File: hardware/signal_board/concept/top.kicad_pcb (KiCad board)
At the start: 2 copper layers, 85 x 115 mm, 288 parts, among them J1 Conn_01x04, J2 USB_OTG, J3 Conn_01x02, J4 Barrel_Jack_Switch, Q1 Q_NMOS_GDS, Q10 Q_NMOS_GDS, Q11 Q_NMOS_GDS, Q12 Q_NMOS_GDS, Q13 Q_NMOS_GDS, Q14 Q_PMOS_GDS, Q15 Q_NMOS_GDS, Q16 Q_PMOS_GDS, Q17 Q_NMOS_GDS, Q18 Q_NMOS_GDS, Q19 Q_NMOS_GDS, Q2 Q_NMOS_GDS, Q20 Q_NMOS_GDS, Q21 Q_NMOS_GDS, Q22 Q_NMOS_GDS, Q3 Q_PMOS_GDS, Q4 Q_NMOS_GDS, Q5 Q_PMOS_GDS, Q6 Q_NMOS_GDS, Q7 Q_NMOS_GDS, Q8 Q_NMOS_GDS, Q9 Q_NMOS_GDS, SW1 SW_Push, SW2 SW_Push, SW3 SW_Push, SW4 SW_Push, U1 STM32F103R(F-G)Tx_u, U10 L5973D, U11 LM3488MM, U12 AMS1117-3.3, U13 AMS1117, U14 LM324, U15 LM324, U16 MCP6001-OT, U17 MCP6001-OT, U18 ADS1118IDGS, U19 LM358, U2 XC6SLX9-TQG144, U20 IR1155S, U21 IR1155S, U22 IR1155S, U23 IR1155S, U3 W25Q32JVSS, U4 MCP6002-xMS, U5 LM324, U6 LM324, U7 MCP6001-OT, U8 MCP6001-OT, U9 ADS1118IDGS, Y1 8MHz

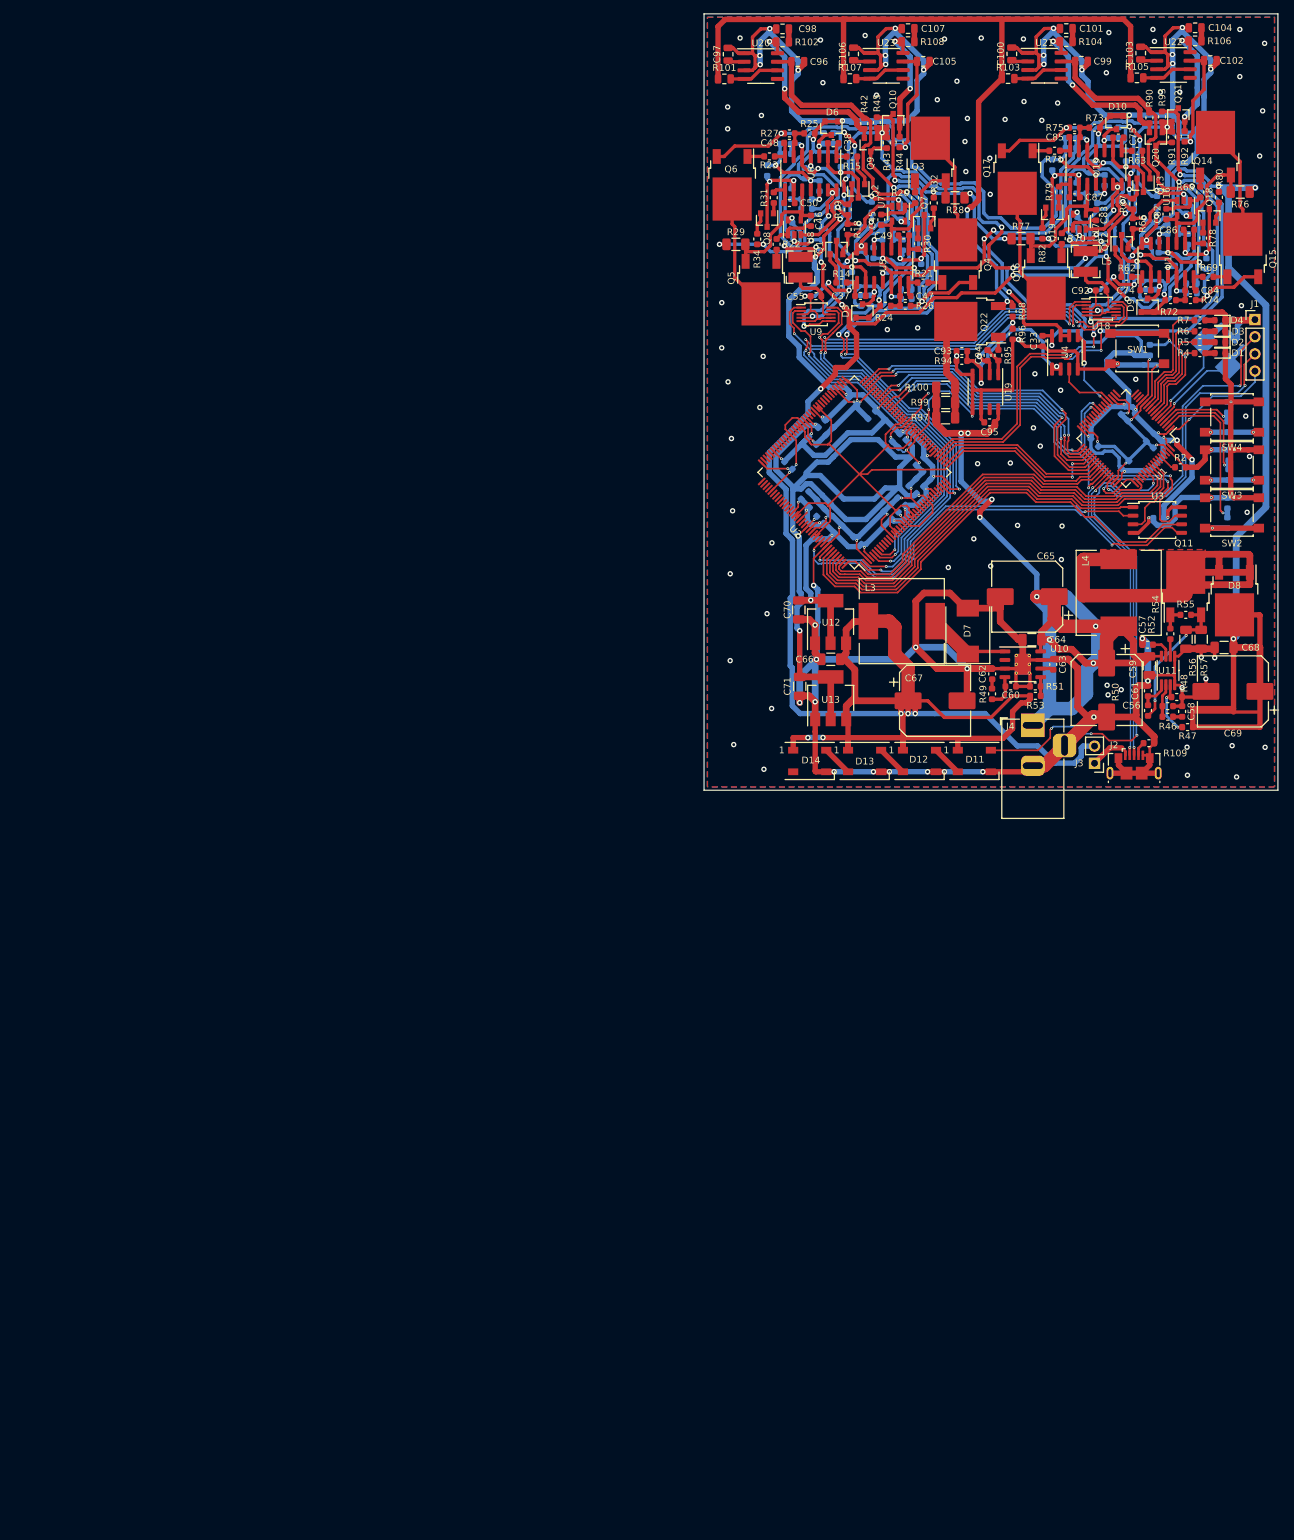
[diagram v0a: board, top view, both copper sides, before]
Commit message: Add priduction board
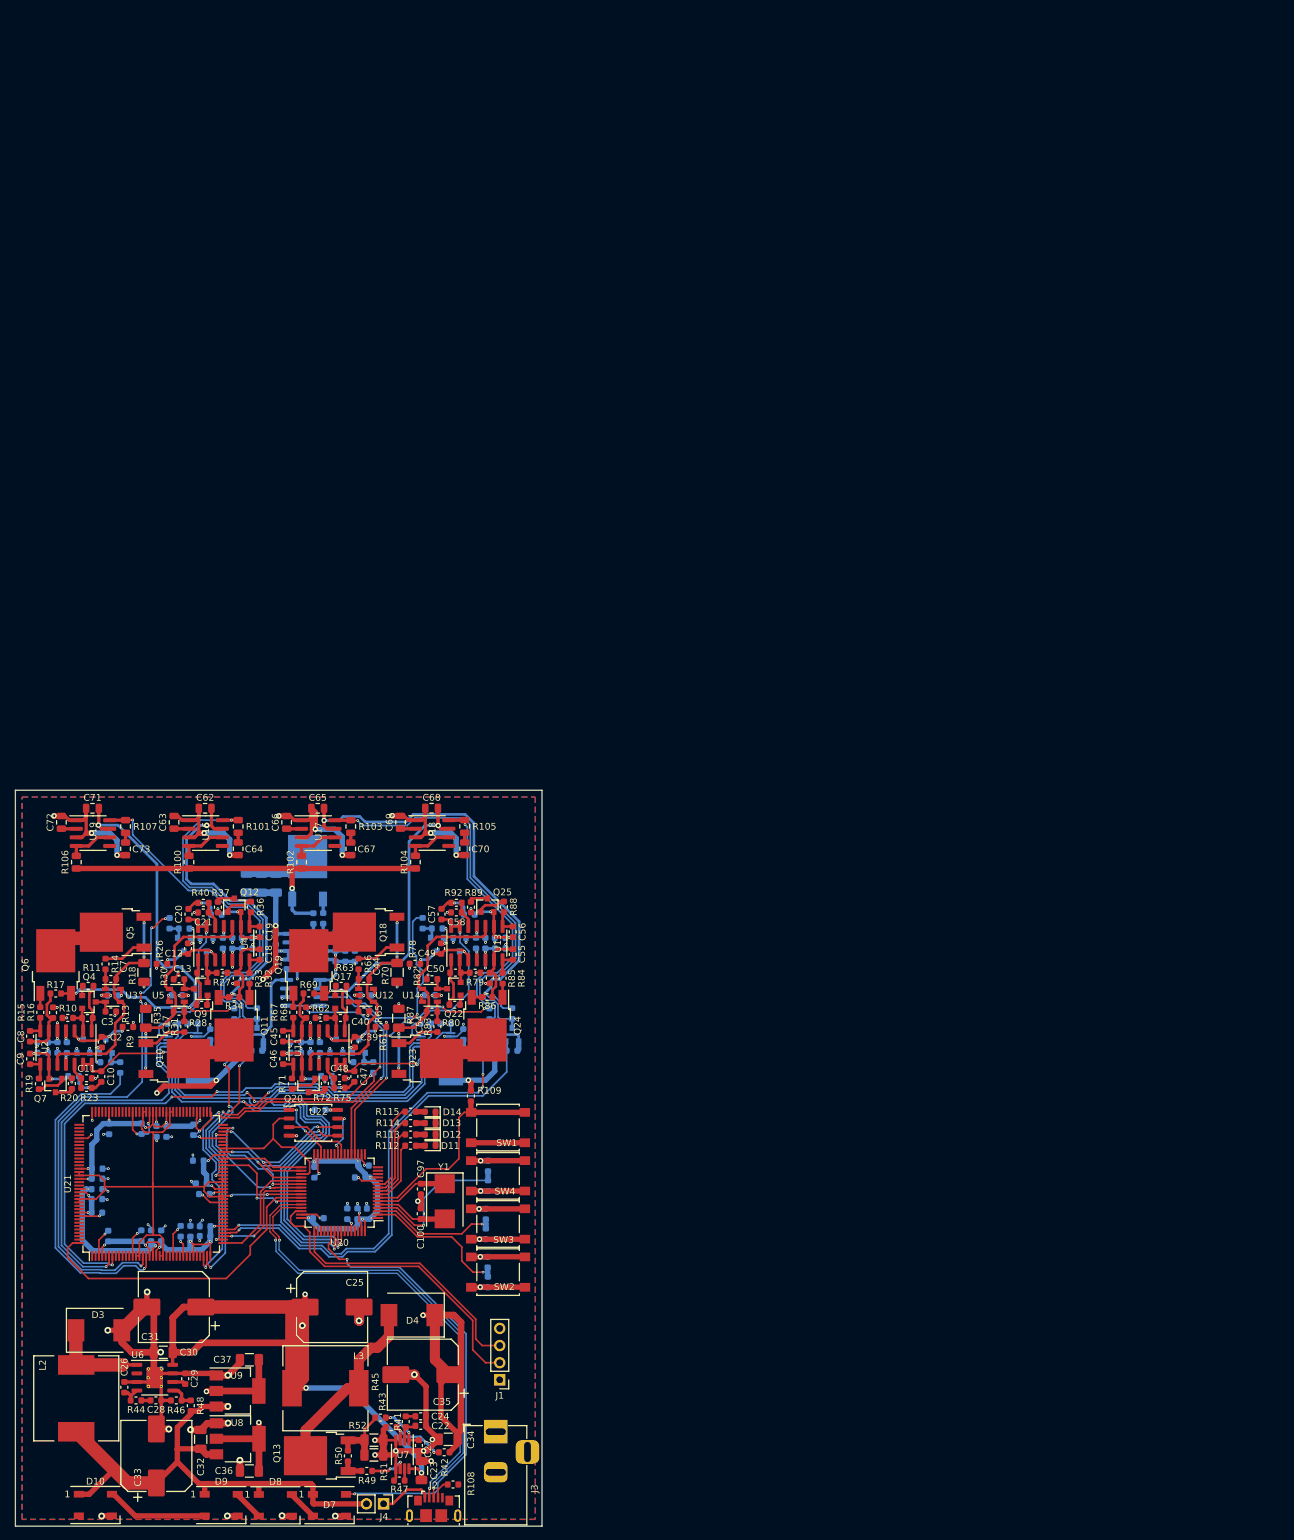
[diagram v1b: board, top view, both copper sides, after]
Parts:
- removed L5: 10u, Inductor_SMD:L_Bourns-SRN4018
- added L1: 10u, Inductor_SMD:L_Bourns-SRN4018, B.Cu at (-0.97, 205.4)
- added Q23: Q_PMOS_GDS, Package_TO_SOT_SMD:TO-252-2, F.Cu at (33.0, 203.7)
- added Q24: Q_NMOS_GDS, Package_TO_SOT_SMD:TO-252-2, F.Cu at (41.9, 198.9)
- added Q25: Q_NMOS_GSD, Package_TO_SOT_SMD:SOT-23, F.Cu at (41.9, 181.0)
- added Q26: Q_NMOS_GDS, Package_TO_SOT_SMD:TO-252-2, B.Cu at (15.3, 175.9)
- added R110: 10k, Resistor_SMD:R_0603_1608Metric, B.Cu at (21.2, 226.7)
- added R111: 1k, Resistor_SMD:R_0603_1608Metric, B.Cu at (42.0, 233.9)
- added R112: 1k, Resistor_SMD:R_0603_1608Metric, F.Cu at (30.5, 216.7)
- added R113: 1k, Resistor_SMD:R_0603_1608Metric, F.Cu at (30.5, 215.0)
- added R114: 1k, Resistor_SMD:R_0603_1608Metric, F.Cu at (30.5, 213.3)
- added R115: 1k, Resistor_SMD:R_0603_1608Metric, F.Cu at (30.5, 211.6)
- added R116: 1k, Resistor_SMD:R_0603_1608Metric, B.Cu at (41.7, 226.8)
- added R117: 1k, Resistor_SMD:R_0603_1608Metric, B.Cu at (42.0, 219.6)
- C10, C20: value 0.1u -> 0.22u; moved to F.Cu
- C100, C97: value 470p -> 10p; footprint Capacitor_SMD:C_0805_2012Metric -> Capacitor_SMD:C_0603_1608Metric
- C101, C104, C107, C98: value 1u -> 0.1u; footprint Capacitor_SMD:C_0805_2012Metric -> Capacitor_SMD:C_0603_1608Metric; moved to B.Cu
- C102, C105, C96, C99: footprint Capacitor_SMD:C_0805_2012Metric -> Capacitor_SMD:C_0603_1608Metric; moved to B.Cu
- C103, C106: value 470p -> 0.1u; footprint Capacitor_SMD:C_0805_2012Metric -> Capacitor_SMD:C_0603_1608Metric; moved to B.Cu
- C11, C12, C2, C21, C28, C29, C39, R10, R13, R36, R61, R84, R85, R89, Y1: moved to F.Cu
- C13, C17, C18, C19, C22, C26, C3, C40, C44, C54, C7, C8, C9: value 0.1u -> 100p; moved to F.Cu
- C23, C30, C32, C34, C36: value 0.1u -> 1u; footprint Capacitor_SMD:C_0603_1608Metric -> Capacitor_SMD:C_1206_3216Metric; moved to F.Cu
- C24, C27: value 10p -> 0.1u; moved to F.Cu
- C25, C31: value 0.1u -> 470u; footprint Capacitor_SMD:C_0603_1608Metric -> Capacitor_SMD:CP_Elec_10x10; moved to F.Cu
- C33: value 0.1u -> 100u; footprint Capacitor_SMD:C_0603_1608Metric -> Capacitor_SMD:CP_Elec_10x10
- C35: value 0.1u -> 100u; footprint Capacitor_SMD:C_0603_1608Metric -> Capacitor_SMD:CP_Elec_10x10; moved to F.Cu
- C37: value 100p -> 1u; footprint Capacitor_SMD:C_0603_1608Metric -> Capacitor_SMD:C_1206_3216Metric
- C38, C74, C75, C82, C83, C84, C85, C86, C87, C94: value 100p -> 0.1u; moved to B.Cu
- C47: value 100p -> 0.22u
- C48, C49: value 100p -> 0.1u
- C51, C52, C88, C89: value 0.22u -> 0.1u
- C55: value 0.1u -> 100p
- C57: value 1u -> 0.22u; footprint Capacitor_SMD:C_1206_3216Metric -> Capacitor_SMD:C_0603_1608Metric
- C59: value 470u -> 0.1u; footprint Capacitor_SMD:CP_Elec_10x10 -> Capacitor_SMD:C_0603_1608Metric; moved to B.Cu
- C60, C61, C92, C93, C95, R2, R22, R90, R95, R99: moved to B.Cu
- C62: footprint Capacitor_SMD:C_0603_1608Metric -> Capacitor_SMD:C_0805_2012Metric
- C63: value 0.1u -> 470p; footprint Capacitor_SMD:C_0603_1608Metric -> Capacitor_SMD:C_0805_2012Metric
- C64, C70: footprint Capacitor_SMD:C_1206_3216Metric -> Capacitor_SMD:C_0805_2012Metric
- C65: value 470u -> 0.1u; footprint Capacitor_SMD:CP_Elec_10x10 -> Capacitor_SMD:C_0805_2012Metric
- C66: value 1u -> 470p; footprint Capacitor_SMD:C_1206_3216Metric -> Capacitor_SMD:C_0805_2012Metric
- C67: value 100u -> 1u; footprint Capacitor_SMD:CP_Elec_10x10 -> Capacitor_SMD:C_0805_2012Metric
- C68, C71: value 1u -> 0.1u; footprint Capacitor_SMD:C_1206_3216Metric -> Capacitor_SMD:C_0805_2012Metric
- C69: value 100u -> 470p; footprint Capacitor_SMD:CP_Elec_10x10 -> Capacitor_SMD:C_0805_2012Metric
- C72: value 0.1u -> 470p; footprint Capacitor_SMD:C_0603_1608Metric -> Capacitor_SMD:C_0805_2012Metric; moved to F.Cu
- C73: value 0.1u -> 1u; footprint Capacitor_SMD:C_0603_1608Metric -> Capacitor_SMD:C_0805_2012Metric; moved to F.Cu
- D1, D2: value LED -> BZX84Cxx; footprint LED_SMD:LED_0603_1608Metric -> Diode_SMD:D_SOT-23_ANK; moved to B.Cu
- D10, D9: value 1.25V -> WS2812B; footprint Package_TO_SOT_SMD:SOT-23 -> LED_SMD:LED_WS2812B_PLCC4_5.0x5.0mm_P3.2mm
- D11, D12, D13, D14: value WS2812B -> LED; footprint LED_SMD:LED_WS2812B_PLCC4_5.0x5.0mm_P3.2mm -> LED_SMD:LED_0603_1608Metric
- D3, D4: value LED -> D_Schottky; footprint LED_SMD:LED_0603_1608Metric -> Diode_SMD:D_SMC
- D5, D6: value 1.25V -> BZX84Cxx; footprint Package_TO_SOT_SMD:SOT-23 -> Diode_SMD:D_SOT-23_ANK; moved to B.Cu
- D7: value D_Schottky -> WS2812B; footprint Diode_SMD:D_SMC -> LED_SMD:LED_WS2812B_PLCC4_5.0x5.0mm_P3.2mm
- D8: value D_Schottky -> WS2812B; footprint Package_TO_SOT_SMD:TO-252-2 -> LED_SMD:LED_WS2812B_PLCC4_5.0x5.0mm_P3.2mm
- J3: value Conn_01x02 -> Barrel_Jack_Switch; footprint Connector_PinHeader_2.54mm:PinHeader_1x02_P2.54mm_Vertical -> Connector_BarrelJack:BarrelJack_Horizontal
- J4: value Barrel_Jack_Switch -> Conn_01x02; footprint Connector_BarrelJack:BarrelJack_Horizontal -> Connector_PinHeader_2.54mm:PinHeader_1x02_P2.54mm_Vertical
- L2: footprint Inductor_SMD:L_Bourns-SRN4018 -> Inductor_SMD:L_12x12mm_H8mm
- L4: footprint Inductor_SMD:L_12x12mm_H8mm -> Inductor_SMD:L_Bourns-SRN4018; moved to B.Cu
- Q1, Q2, Q21, Q8: value Q_NMOS_GDS -> Q_NMOS_GSD; moved to B.Cu
- Q10, Q18: value Q_NMOS_GDS -> Q_PMOS_GDS; footprint Package_TO_SOT_SMD:SOT-23 -> Package_TO_SOT_SMD:TO-252-2
- Q12, Q20, Q7, Q9: value Q_NMOS_GDS -> Q_NMOS_GSD
- Q13, Q19: footprint Package_TO_SOT_SMD:SOT-23 -> Package_TO_SOT_SMD:TO-252-2
- Q14, Q16, Q3: value Q_PMOS_GDS -> Q_NMOS_GSD; footprint Package_TO_SOT_SMD:TO-252-2 -> Package_TO_SOT_SMD:SOT-23; moved to B.Cu
- Q15: value Q_NMOS_GDS -> Q_NMOS_GSD; footprint Package_TO_SOT_SMD:TO-252-2 -> Package_TO_SOT_SMD:SOT-23; moved to B.Cu
- Q17, Q22, Q4: value Q_NMOS_GDS -> Q_NMOS_GSD; footprint Package_TO_SOT_SMD:TO-252-2 -> Package_TO_SOT_SMD:SOT-23
- R100: value 100 -> 470; footprint Resistor_SMD:R_1206_3216Metric -> Resistor_SMD:R_0805_2012Metric
- R101, R103, R105, R107: value 470 -> 10k
- R102, R104, R106: value 10k -> 470
- R108: value 10k -> 1k; footprint Resistor_SMD:R_0805_2012Metric -> Resistor_SMD:R_0603_1608Metric
- R109, R20, R3, R30, R38, R62, R72, R78, R79, R8: value 1k -> 10k
- R11, R33, R40, R41, R83, R88: value 10k -> 1k; moved to F.Cu
- R12, R81: value 10k -> 100k
- R16: value 100k -> 1k; moved to F.Cu
- R17: value 100k -> 9.1k; moved to F.Cu
- R18: value 10k -> 1k; footprint Resistor_SMD:R_0603_1608Metric -> Resistor_SMD:R_1206_3216Metric
- R19, R32, R44, R66, R67, R80, R92: value 10k -> 1k
- R21, R25, R4, R5, R6, R73: value 1k -> 10k; moved to B.Cu
- R24, R7: value 1k -> 100; moved to B.Cu
- R26, R27: value 9.1k -> 10k
- R28: footprint Resistor_SMD:R_1206_3216Metric -> Resistor_SMD:R_0603_1608Metric
- R29: value 1k -> 100k; footprint Resistor_SMD:R_1206_3216Metric -> Resistor_SMD:R_0603_1608Metric; moved to B.Cu
- R34: value 10k -> 9.1k
- R35: value 10k -> 1k; footprint Resistor_SMD:R_0603_1608Metric -> Resistor_SMD:R_1206_3216Metric; moved to F.Cu
- R37, R9: value 1k -> 10k; moved to F.Cu
- R42, R43, R45: value 10k -> 10K
- R46: value 1k -> 10K
- R49: value 1k -> 22
- R51, R52: value 10K -> 0.1; footprint Resistor_SMD:R_0603_1608Metric -> Resistor_SMD:R_1206_3216Metric
- R53, R55: value 10K -> 10k; moved to B.Cu
- R54: value 22 -> 10k; moved to B.Cu
- R56, R57: value 0.1 -> 10k; footprint Resistor_SMD:R_1206_3216Metric -> Resistor_SMD:R_0603_1608Metric; moved to B.Cu
- R59: value 10k -> 100
- R65: value 100k -> 10k; moved to F.Cu
- R69: value 1k -> 9.1k
- R70: footprint Resistor_SMD:R_0603_1608Metric -> Resistor_SMD:R_1206_3216Metric
- R74: value 9.1k -> 1k; moved to B.Cu
- R75: value 9.1k -> 1k
- R76: value 1k -> 100; footprint Resistor_SMD:R_1206_3216Metric -> Resistor_SMD:R_0603_1608Metric; moved to B.Cu
- R77: value 1k -> 10k; footprint Resistor_SMD:R_1206_3216Metric -> Resistor_SMD:R_0603_1608Metric; moved to B.Cu
- R86: value 1k -> 9.1k; moved to F.Cu
- R87: footprint Resistor_SMD:R_0603_1608Metric -> Resistor_SMD:R_1206_3216Metric; moved to F.Cu
- R91: value 10k -> 1k; moved to B.Cu
- R93: value 10k -> 100k; moved to B.Cu
- R94: value 100k -> 1k; moved to B.Cu
- R96, R98: value 1k -> 100; footprint Resistor_SMD:R_0603_1608Metric -> Resistor_SMD:R_1206_3216Metric; moved to B.Cu
- R97: value 100 -> 1k; footprint Resistor_SMD:R_1206_3216Metric -> Resistor_SMD:R_0603_1608Metric; moved to B.Cu
- U1: value STM32F103R(F-G)Tx_u -> ADS1118IDGS; footprint Package_QFP:LQFP-64_10x10mm_P0.5mm -> Package_SO:MSOP-10_3x3mm_P0.5mm; moved to B.Cu
- U10: value L5973D -> ADS1118IDGS; footprint Package_SO:HSOP-8-1EP_3.9x4.9mm_P1.27mm_EP2.41x3.1mm_ThermalVias -> Package_SO:MSOP-10_3x3mm_P0.5mm; moved to B.Cu
- U11: value LM3488MM -> LM324; footprint Package_SO:MSOP-8_3x3mm_P0.65mm -> Package_SO:SOIC-14_3.9x8.7mm_P1.27mm
- U12: value AMS1117-3.3 -> MCP6001-OT; footprint Package_TO_SOT_SMD:SOT-223-3_TabPin2 -> Package_TO_SOT_SMD:SOT-23-5
- U13: value AMS1117 -> LM324; footprint Package_TO_SOT_SMD:SOT-223-3_TabPin2 -> Package_SO:SOIC-14_3.9x8.7mm_P1.27mm
- U14, U5: value LM324 -> MCP6001-OT; footprint Package_SO:SOIC-14_3.9x8.7mm_P1.27mm -> Package_TO_SOT_SMD:SOT-23-5
- U15: value LM324 -> LM358; footprint Package_SO:SOIC-14_3.9x8.7mm_P1.27mm -> Package_SO:SO-8_3.9x4.9mm_P1.27mm; moved to B.Cu
- U16, U17: value MCP6001-OT -> IR1155S; footprint Package_TO_SOT_SMD:SOT-23-5 -> Package_SO:SOIC-8_3.9x4.9mm_P1.27mm
- U18: value ADS1118IDGS -> IR1155S; footprint Package_SO:MSOP-10_3x3mm_P0.5mm -> Package_SO:SOIC-8_3.9x4.9mm_P1.27mm
- U19: value LM358 -> IR1155S; footprint Package_SO:SO-8_3.9x4.9mm_P1.27mm -> Package_SO:SOIC-8_3.9x4.9mm_P1.27mm
- U2: value XC6SLX9-TQG144 -> LM324; footprint Package_QFP:TQFP-144_20x20mm_P0.5mm -> Package_SO:SOIC-14_3.9x8.7mm_P1.27mm
- U20: value IR1155S -> STM32F103R(F-G)Tx_u; footprint Package_SO:SOIC-8_3.9x4.9mm_P1.27mm -> Package_QFP:LQFP-64_10x10mm_P0.5mm
- U21: value IR1155S -> XC6SLX9-TQG144; footprint Package_SO:SOIC-8_3.9x4.9mm_P1.27mm -> Package_QFP:TQFP-144_20x20mm_P0.5mm
- U22: value IR1155S -> W25Q32JVSS; footprint Package_SO:SOIC-8_3.9x4.9mm_P1.27mm -> Package_SO:SOIC-8_5.23x5.23mm_P1.27mm
- U23: value IR1155S -> MCP6002-xMS; moved to B.Cu
- U3: value W25Q32JVSS -> MCP6001-OT; footprint Package_SO:SOIC-8_5.23x5.23mm_P1.27mm -> Package_TO_SOT_SMD:SOT-23-5
- U4: value MCP6002-xMS -> LM324; footprint Package_SO:SOIC-8_3.9x4.9mm_P1.27mm -> Package_SO:SOIC-14_3.9x8.7mm_P1.27mm
- U6: value LM324 -> L5973D; footprint Package_SO:SOIC-14_3.9x8.7mm_P1.27mm -> Package_SO:HSOP-8-1EP_3.9x4.9mm_P1.27mm_EP2.41x3.1mm_ThermalVias
- U7: value MCP6001-OT -> LM3488MM; footprint Package_TO_SOT_SMD:SOT-23-5 -> Package_SO:MSOP-8_3x3mm_P0.65mm
- U8: value MCP6001-OT -> AMS1117-3.3; footprint Package_TO_SOT_SMD:SOT-23-5 -> Package_TO_SOT_SMD:SOT-223-3_TabPin2
- U9: value ADS1118IDGS -> AMS1117; footprint Package_SO:MSOP-10_3x3mm_P0.5mm -> Package_TO_SOT_SMD:SOT-223-3_TabPin2
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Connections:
- C1 pad 1: /VDD3.3V -> Net-(C1-Pad1)
- C10 pad 1: /VDD1.25V -> /Cell_0_Sheet/CurrentSource_B_Sheet/PFC_CRNT
- C10 pad 2: GNDA -> Net-(C10-Pad2)
- C101 pad 1: Net-(C101-Pad1) -> /CoreSheet/STM32F103_BTN_0
- C102 pad 1: /PFC_VCC_DUT_3 -> /VDD3.3V
- C103 pad 1: Net-(C103-Pad1) -> /VDD3.3V
- C104 pad 1: Net-(C104-Pad1) -> /VDD3.3V
- C105 pad 1: /PFC_VCC_DUT_1 -> /CoreSheet/STM32F103_BTN_1
- C106 pad 1: Net-(C106-Pad1) -> /VDD3.3V
- C107 pad 1: Net-(C107-Pad1) -> /CoreSheet/STM32F103_BTN_2
- C11 pad 1: /VDD3.3V -> Net-(C11-Pad1)
- C12 pad 1: /VDD3.3V -> Net-(C12-Pad1)
- C13 pad 1: /VDD1.25V -> Net-(C13-Pad1)
- C13 pad 2: GNDA -> Net-(C13-Pad2)
- C14 pad 1: /VDD3.3V -> /VCC30V
- C15 pad 1: /VDD3.3V -> /VCC5V
- C16 pad 1: /VDD1.25V -> /U_PFC_VCC_ADJ
- C17 pad 1: /VDD3.3V -> Net-(C17-Pad1)
- C17 pad 2: GNDA -> Net-(C17-Pad2)
- C18 pad 1: /VDD3.3V -> Net-(C18-Pad1)
- C18 pad 2: GNDA -> Net-(C18-Pad2)
- C19 pad 1: /VDD3.3V -> Net-(C19-Pad1)
- C19 pad 2: GNDA -> Net-(C19-Pad2)
- C2 pad 1: /VDD3.3V -> Net-(C2-Pad1)
- C20 pad 1: /VDD3.3V -> /Cell_0_Sheet/CurrentSource_A_Sheet/PFC_CRNT
- C20 pad 2: GNDA -> Net-(C20-Pad2)
- C21 pad 1: /VDD3.3V -> Net-(C21-Pad1)
- C22 pad 1: /VDD3.3V -> Net-(C22-Pad1)
- C23 pad 1: /VDD3.3V -> /VCC12V
- C25 pad 1: /VDD3.3V -> /VCC12V
- C26 pad 1: /VDD3.3V -> Net-(C26-Pad1)
- C28 pad 1: /CoreSheet/STM32F103_BTN_0 -> Net-(C28-Pad1)
- C29 pad 1: /VDD3.3V -> Net-(C29-Pad1)
- C3 pad 1: /VDD3.3V -> Net-(C3-Pad1)
- C3 pad 2: GNDA -> Net-(C3-Pad2)
- C30 pad 1: /VDD3.3V -> /VCC12V
- C31 pad 1: /VDD3.3V -> /VCC12V
- C32 pad 1: /CoreSheet/STM32F103_BTN_1 -> /VCC5V
- C33 pad 1: /VDD3.3V -> /VCC5V
- C34 pad 1: /CoreSheet/STM32F103_BTN_2 -> /VCC30V
- C35 pad 1: Net-(C35-Pad1) -> /VCC30V
- C36 pad 1: Net-(C36-Pad1) -> /VDD3.3V
- C37 pad 1: Net-(C37-Pad1) -> GNDA
- C37 pad 2: Net-(C37-Pad2) -> /VDD1.25V
- C38 pad 2: Net-(C38-Pad2) -> GNDA
- C39 pad 1: /VCC30V -> Net-(C39-Pad1)
- C4 pad 1: /VDD1.25V -> /VCC30V
- C40 pad 1: /VCC5V -> Net-(C40-Pad1)
- C40 pad 2: GNDA -> Net-(C40-Pad2)
- C44 pad 1: /U_PFC_VCC_ADJ -> Net-(C44-Pad1)
- C44 pad 2: GNDA -> Net-(C44-Pad2)
- C47 pad 1: Net-(C47-Pad1) -> /Cell_1_Sheet/CurrentSource_B_Sheet/PFC_CRNT
- C48 pad 2: Net-(C48-Pad2) -> GNDA
- C49 pad 2: Net-(C49-Pad2) -> GNDA
- C5 pad 1: /VDD3.3V -> /VCC5V
- C51 pad 1: Net-(C51-Pad1) -> /VCC30V
- C51 pad 2: Net-(C51-Pad2) -> GNDA
- C52 pad 1: Net-(C52-Pad1) -> /VCC5V
- C52 pad 2: Net-(C52-Pad2) -> GNDA
- C53 pad 1: Net-(C53-Pad1) -> /U_PFC_VCC_ADJ
- C54 pad 2: GNDA -> Net-(C54-Pad2)
- C55 pad 2: GNDA -> Net-(C55-Pad2)
- C56 pad 2: GNDA -> Net-(C56-Pad2)
- C57 pad 1: /VCC12V -> /Cell_1_Sheet/CurrentSource_A_Sheet/PFC_CRNT
- C57 pad 2: GNDA -> Net-(C57-Pad2)
- C59 pad 1: /VCC12V -> /U_PFC_FB_OVP_ADJ
- C6 pad 1: /VDD3.3V -> /U_PFC_VCC_ADJ
- C60 pad 2: GNDA -> Net-(C60-Pad2)
- C61 pad 1: Net-(C61-Pad1) -> /VCC12V
- C62 pad 1: Net-(C62-Pad1) -> /PFC_VCC_DUT_0
- C64 pad 1: /VCC12V -> Net-(C64-Pad1)
- C65 pad 1: /VCC12V -> /PFC_VCC_DUT_2
- C66 pad 1: /VCC5V -> Net-(C66-Pad1)
- C67 pad 1: /VCC5V -> Net-(C67-Pad1)
- C68 pad 1: /VCC30V -> /PFC_VCC_DUT_3
- C69 pad 1: /VCC30V -> Net-(C69-Pad1)
- C7 pad 1: /VDD1.25V -> Net-(C7-Pad1)
- C7 pad 2: GNDA -> Net-(C7-Pad2)
- C70 pad 1: /VDD3.3V -> Net-(C70-Pad1)
- C71 pad 1: GNDA -> /PFC_VCC_DUT_1
- C71 pad 2: /VDD1.25V -> GNDA
- C74 pad 1: Net-(C74-Pad1) -> /VDD3.3V
- C74 pad 2: Net-(C74-Pad2) -> GNDA
- C75 pad 1: Net-(C75-Pad1) -> /VDD3.3V
- C75 pad 2: Net-(C75-Pad2) -> GNDA
- C76 pad 1: /VCC30V -> /VDD3.3V
- C77 pad 1: /VCC5V -> /VDD1.25V
- C78 pad 1: /VCC30V -> /VDD3.3V
- C79 pad 1: /VCC5V -> /VDD3.3V
- C8 pad 1: /VDD3.3V -> Net-(C8-Pad1)
- C8 pad 2: GNDA -> Net-(C8-Pad2)
- C80 pad 1: /U_PFC_VCC_ADJ -> /VDD1.25V
- C81 pad 1: /U_PFC_VCC_ADJ -> /VDD3.3V
- C82 pad 1: Net-(C82-Pad1) -> /VDD3.3V
- C82 pad 2: Net-(C82-Pad2) -> GNDA
- C83 pad 1: Net-(C83-Pad1) -> /VDD1.25V
- C83 pad 2: Net-(C83-Pad2) -> GNDA
- C84 pad 1: Net-(C84-Pad1) -> /VDD3.3V
- C84 pad 2: Net-(C84-Pad2) -> GNDA
- C85 pad 1: Net-(C85-Pad1) -> /VDD3.3V
- C85 pad 2: Net-(C85-Pad2) -> GNDA
- C86 pad 1: Net-(C86-Pad1) -> /VDD1.25V
- C86 pad 2: Net-(C86-Pad2) -> GNDA
- C87 pad 1: Net-(C87-Pad1) -> /VDD3.3V
- C87 pad 2: Net-(C87-Pad2) -> GNDA
- C88 pad 1: Net-(C88-Pad1) -> /VDD3.3V
- C88 pad 2: Net-(C88-Pad2) -> GNDA
- C89 pad 1: Net-(C89-Pad1) -> /VDD1.25V
- C89 pad 2: Net-(C89-Pad2) -> GNDA
- C9 pad 1: /VDD3.3V -> Net-(C9-Pad1)
- C9 pad 2: GNDA -> Net-(C9-Pad2)
- C90 pad 1: Net-(C90-Pad1) -> /VDD3.3V
- C91 pad 1: Net-(C91-Pad1) -> /VDD3.3V
- C92 pad 1: Net-(C92-Pad1) -> /VDD3.3V
- C93 pad 1: /U_PFC_FB_OVP_ADJ -> /VDD3.3V
- C94 pad 1: Net-(C94-Pad1) -> /VDD3.3V
- C94 pad 2: Net-(C94-Pad2) -> GNDA
- C95 pad 1: /VCC12V -> /VDD3.3V
- C96 pad 1: /PFC_VCC_DUT_0 -> /VDD3.3V
- C98 pad 1: Net-(C98-Pad1) -> /VDD3.3V
- C99 pad 1: /PFC_VCC_DUT_2 -> /VDD3.3V
- D1 pad 1: GNDA -> Net-(C2-Pad1)
- D1 pad 2: Net-(D1-Pad2) -> GNDA
- D10 pad 1: Net-(C73-Pad1) -> /VCC5V
- D10 pad 2: GNDA -> (no net)
- D11 pad 1: /VCC5V -> GNDA
- D12 pad 1: /VCC5V -> GNDA
- D13 pad 1: /VCC5V -> GNDA
- D14 pad 1: /VCC5V -> GNDA
- D14 pad 2: (no net) -> Net-(D14-Pad2)
- D2 pad 1: GNDA -> Net-(C12-Pad1)
- D2 pad 2: Net-(D2-Pad2) -> GNDA
- D3 pad 1: GNDA -> Net-(D3-Pad1)
- D3 pad 2: Net-(D3-Pad2) -> GNDA
- D4 pad 1: GNDA -> /VCC30V
- D5 pad 1: Net-(C35-Pad1) -> Net-(C39-Pad1)
- D6 pad 1: Net-(C36-Pad1) -> Net-(C49-Pad1)
- D7 pad 1: Net-(D7-Pad1) -> /VCC5V
- D7 pad 2: GNDA -> Net-(D7-Pad2)
- D8 pad 1: /VCC30V -> /VCC5V
- D9 pad 1: Net-(C72-Pad1) -> /VCC5V
- D9 pad 2: GNDA -> Net-(D10-Pad4)
- J3 pad 1: Net-(J2-Pad1) -> /VCC12V
- J3 pad 2: /VCC5V -> GNDA
- J4 pad 1: /VCC12V -> Net-(J2-Pad1)
- J4 pad 2: GNDA -> /VCC5V
- L2 pad 1: Net-(C55-Pad1) -> Net-(D3-Pad1)
- L2 pad 2: /VDD3.3V -> /VCC5V
- L3 pad 1: Net-(D7-Pad1) -> /VCC12V
- L3 pad 2: /VCC5V -> Net-(D4-Pad2)
- L4 pad 1: /VCC12V -> Net-(C38-Pad1)
- L4 pad 2: Net-(D8-Pad2) -> /VDD3.3V
- Q1 pad 1: Net-(Q1-Pad1) -> /VDD3.3V
- Q1 pad 2: Net-(Q1-Pad2) -> /PFC_GATE_LOW_0
- Q1 pad 3: Net-(C37-Pad2) -> /PFC_GATE_HIGH_0
- Q10 pad 1: /VDD3.3V -> Net-(Q10-Pad1)
- Q10 pad 2: /PFC_GATE_HIGH_1 -> Net-(Q10-Pad2)
- Q10 pad 3: /PFC_GATE_LOW_1 -> Net-(C17-Pad2)
- Q11 pad 2: Net-(D8-Pad2) -> Net-(Q10-Pad2)
- Q11 pad 3: Net-(Q11-Pad3) -> /PFC_VCC_DUT_0
- Q12 pad 2: Net-(Q12-Pad2) -> Net-(C19-Pad2)
- Q12 pad 3: Net-(C74-Pad2) -> Net-(Q12-Pad3)
- Q13 pad 2: Net-(Q13-Pad2) -> Net-(D4-Pad2)
- Q13 pad 3: Net-(C75-Pad2) -> Net-(Q13-Pad3)
- Q14 pad 1: Net-(Q14-Pad1) -> /VDD3.3V
- Q14 pad 2: Net-(Q14-Pad2) -> /PFC_GATE_LOW_2
- Q14 pad 3: Net-(C82-Pad2) -> /PFC_GATE_HIGH_2
- Q15 pad 1: Net-(Q15-Pad1) -> /VDD3.3V
- Q15 pad 2: Net-(Q14-Pad2) -> /PFC_GATE_LOW_3
- Q15 pad 3: /PFC_VCC_DUT_2 -> /PFC_GATE_HIGH_3
- Q16 pad 2: Net-(Q16-Pad2) -> GNDA
- Q16 pad 3: Net-(C83-Pad2) -> Net-(C39-Pad1)
- Q17 pad 2: Net-(Q16-Pad2) -> Net-(C40-Pad2)
- Q17 pad 3: /PFC_VCC_DUT_3 -> Net-(Q17-Pad3)
- Q18 pad 3: Net-(C86-Pad2) -> Net-(C44-Pad2)
- Q19 pad 2: Net-(Q19-Pad2) -> Net-(Q18-Pad2)
- Q19 pad 3: Net-(C87-Pad2) -> /PFC_VCC_DUT_3
- Q2 pad 1: Net-(Q2-Pad1) -> /VDD3.3V
- Q2 pad 2: Net-(Q2-Pad2) -> /PFC_GATE_LOW_1
- Q2 pad 3: Net-(C38-Pad2) -> /PFC_GATE_HIGH_1
- Q20 pad 1: /VDD3.3V -> Net-(Q20-Pad1)
- Q20 pad 2: /PFC_GATE_HIGH_2 -> Net-(C46-Pad2)
- Q20 pad 3: /PFC_GATE_LOW_2 -> Net-(Q20-Pad3)
- Q21 pad 1: /VDD3.3V -> Net-(Q21-Pad1)
- Q21 pad 2: /PFC_GATE_HIGH_3 -> GNDA
- Q21 pad 3: /PFC_GATE_LOW_3 -> Net-(C49-Pad1)
- Q22 pad 2: Net-(Q22-Pad2) -> Net-(C50-Pad2)
- Q22 pad 3: /PFC_DUT_FB_OVP -> Net-(Q22-Pad3)
- Q3 pad 2: Net-(Q3-Pad2) -> GNDA
- Q3 pad 3: Net-(C45-Pad2) -> Net-(C2-Pad1)
- Q4 pad 2: Net-(Q3-Pad2) -> Net-(C3-Pad2)
- Q4 pad 3: /PFC_VCC_DUT_0 -> Net-(Q4-Pad3)
- Q5 pad 3: Net-(C46-Pad2) -> Net-(C7-Pad2)
- Q7 pad 2: Net-(Q7-Pad2) -> Net-(C9-Pad2)
- Q7 pad 3: Net-(C49-Pad2) -> Net-(Q7-Pad3)
- Q8 pad 2: Net-(Q8-Pad2) -> GNDA
- Q8 pad 3: Net-(C50-Pad2) -> Net-(C12-Pad1)
- Q9 pad 1: /VDD3.3V -> Net-(Q9-Pad1)
- Q9 pad 2: /PFC_GATE_HIGH_0 -> Net-(C13-Pad2)
- Q9 pad 3: /PFC_GATE_LOW_0 -> Net-(Q9-Pad3)
- R1 pad 1: /VDD3.3V -> /Cell_0_Sheet/CurrentSource_A_Sheet/PFC_CRNT
- R1 pad 2: Net-(R1-Pad2) -> GNDA
- R10 pad 1: Net-(C35-Pad1) -> Net-(C3-Pad2)
- R10 pad 2: /VCC5V -> GNDA
- R100 pad 1: /VCC12V -> /PFC_DUT_FB_OVP
- R100 pad 2: Net-(Q22-Pad2) -> Net-(R100-Pad2)
- R101 pad 1: /PFC_DUT_FB_OVP -> /PFC_GATE_HIGH_0
- R101 pad 2: Net-(R101-Pad2) -> Net-(C64-Pad1)
- R102 pad 1: /PFC_GATE_HIGH_0 -> /PFC_DUT_FB_OVP
- R102 pad 2: Net-(C98-Pad1) -> Net-(R102-Pad2)
- R103 pad 1: /PFC_DUT_FB_OVP -> /PFC_GATE_HIGH_2
- R103 pad 2: Net-(R103-Pad2) -> Net-(C67-Pad1)
- R104 pad 1: /PFC_GATE_HIGH_2 -> /PFC_DUT_FB_OVP
- R104 pad 2: Net-(C101-Pad1) -> Net-(R104-Pad2)
- R105 pad 1: /PFC_DUT_FB_OVP -> /PFC_GATE_HIGH_3
- R105 pad 2: Net-(R105-Pad2) -> Net-(C70-Pad1)
- R106 pad 1: /PFC_GATE_HIGH_3 -> /PFC_DUT_FB_OVP
- R106 pad 2: Net-(C104-Pad1) -> Net-(R106-Pad2)
- R107 pad 1: /PFC_DUT_FB_OVP -> /PFC_GATE_HIGH_1
- R107 pad 2: Net-(R107-Pad2) -> Net-(C73-Pad1)
- R108 pad 1: /PFC_GATE_HIGH_1 -> Net-(J2-Pad4)
- R108 pad 2: Net-(C107-Pad1) -> GNDA
- R109 pad 1: Net-(J2-Pad4) -> /VDD3.3V
- R109 pad 2: GNDA -> Net-(R109-Pad2)
- R11 pad 1: Net-(C36-Pad1) -> Net-(Q4-Pad1)
- R11 pad 2: /VCC5V -> Net-(C3-Pad1)
- R12 pad 1: Net-(C37-Pad2) -> /U_PFC_VCC_ADJ
- R13 pad 1: Net-(C38-Pad2) -> /VCC30V
- R13 pad 2: GNDA -> Net-(Q4-Pad3)
- R14 pad 1: Net-(Q1-Pad1) -> Net-(Q5-Pad1)
- R14 pad 2: Net-(C37-Pad1) -> Net-(C7-Pad1)
- R15 pad 1: Net-(Q2-Pad1) -> Net-(Q6-Pad1)
- R15 pad 2: Net-(C38-Pad1) -> Net-(C8-Pad1)
- R16 pad 1: /U_PFC_VCC_ADJ -> Net-(C8-Pad2)
- R17 pad 1: /U_PFC_VCC_ADJ -> /PFC_VCC_DUT_1
- R17 pad 2: GNDA -> Net-(C8-Pad2)
- R18 pad 2: Net-(Q1-Pad2) -> Net-(C7-Pad2)
- R19 pad 1: /VCC30V -> Net-(Q7-Pad1)
- R19 pad 2: Net-(Q2-Pad2) -> Net-(C9-Pad1)
- R2 pad 1: Net-(R2-Pad1) -> /Cell_0_Sheet/CurrentSource_B_Sheet/PFC_CRNT
- R20 pad 1: Net-(Q3-Pad1) -> /VCC30V
- R20 pad 2: Net-(C45-Pad1) -> Net-(Q7-Pad3)
- R21 pad 1: Net-(Q4-Pad1) -> Net-(C9-Pad2)
- R21 pad 2: Net-(C47-Pad1) -> GNDA
- R22 pad 1: Net-(Q5-Pad1) -> Net-(C10-Pad2)
- R22 pad 2: Net-(C46-Pad1) -> Net-(C9-Pad2)
- R23 pad 1: Net-(Q6-Pad1) -> Net-(C11-Pad1)
- R23 pad 2: Net-(C48-Pad1) -> Net-(C10-Pad2)
- R24 pad 1: Net-(C47-Pad2) -> /PFC_STOP_0
- R24 pad 2: GNDA -> Net-(Q8-Pad1)
- R25 pad 1: Net-(C48-Pad2) -> Net-(Q8-Pad1)
- R26 pad 1: /PFC_VCC_DUT_0 -> Net-(C12-Pad1)
- R26 pad 2: Net-(C47-Pad2) -> /VCC5V
- R27 pad 1: /PFC_VCC_DUT_1 -> Net-(C13-Pad2)
- R27 pad 2: Net-(C48-Pad2) -> GNDA
- R28 pad 1: /VCC30V -> Net-(Q9-Pad1)
- R28 pad 2: Net-(C45-Pad2) -> Net-(C13-Pad1)
- R29 pad 1: /VCC30V -> /U_PFC_VCC_ADJ
- R29 pad 2: Net-(C46-Pad2) -> GNDA
- R3 pad 1: /CoreSheet/STM32F103_BTN_0 -> /PFC_GATE_HIGH_0
- R3 pad 2: Net-(R3-Pad2) -> /PFC_VCC_DUT_0
- R30 pad 1: Net-(Q7-Pad1) -> /VCC30V
- R30 pad 2: Net-(C49-Pad1) -> Net-(Q9-Pad3)
- R31 pad 1: Net-(Q8-Pad1) -> Net-(Q10-Pad1)
- R31 pad 2: Net-(C50-Pad1) -> Net-(C17-Pad1)
- R32 pad 1: /VCC30V -> Net-(Q11-Pad1)
- R32 pad 2: Net-(Q7-Pad2) -> Net-(C18-Pad1)
- R33 pad 1: Net-(C49-Pad2) -> Net-(C18-Pad2)
- R34 pad 1: /VCC30V -> /PFC_VCC_DUT_0
- R34 pad 2: Net-(Q8-Pad2) -> Net-(C18-Pad2)
- R35 pad 1: Net-(C50-Pad2) -> /VCC30V
- R35 pad 2: GNDA -> Net-(C17-Pad2)
- R36 pad 1: Net-(C51-Pad2) -> Net-(Q12-Pad1)
- R36 pad 2: Net-(C49-Pad2) -> Net-(C19-Pad1)
- R37 pad 1: Net-(C52-Pad2) -> /VCC30V
- R37 pad 2: Net-(C50-Pad2) -> Net-(Q12-Pad3)
- R38 pad 1: Net-(C53-Pad1) -> Net-(C19-Pad2)
- R38 pad 2: Net-(C51-Pad2) -> GNDA
- R39 pad 1: Net-(C54-Pad1) -> Net-(C20-Pad2)
- R39 pad 2: Net-(C52-Pad2) -> Net-(C19-Pad2)
- R4 pad 1: /CoreSheet/STM32F103_SIG_LED_0 -> /PFC_GATE_LOW_0
- R4 pad 2: Net-(D1-Pad2) -> /VDD3.3V
- R40 pad 1: Net-(C51-Pad1) -> Net-(C21-Pad1)
- R40 pad 2: GNDA -> Net-(C20-Pad2)
- R41 pad 1: Net-(C52-Pad1) -> Net-(C24-Pad1)
- R41 pad 2: GNDA -> Net-(C22-Pad1)
- R42 pad 1: /PFC_GATE_HIGH_0 -> Net-(R42-Pad1)
- R42 pad 2: /PFC_VCC_DUT_0 -> /VCC30V
- R43 pad 1: /PFC_GATE_LOW_0 -> GNDA
- R43 pad 2: /VDD3.3V -> Net-(R42-Pad1)
- R44 pad 1: /PFC_GATE_HIGH_1 -> Net-(C28-Pad1)
- R44 pad 2: /PFC_VCC_DUT_1 -> Net-(C26-Pad1)
- R45 pad 1: /PFC_GATE_LOW_1 -> Net-(C27-Pad1)
- R45 pad 2: /VDD3.3V -> Net-(Q13-Pad3)
- R46 pad 1: Net-(C58-Pad1) -> GNDA
- R46 pad 2: Net-(C56-Pad1) -> Net-(R46-Pad2)
- R47 pad 1: Net-(R47-Pad1) -> GNDA
- R47 pad 2: /VCC30V -> Net-(R47-Pad2)
- R48 pad 1: GNDA -> Net-(R46-Pad2)
- R48 pad 2: Net-(R47-Pad1) -> /VCC5V
- R49 pad 1: Net-(C62-Pad1) -> Net-(R49-Pad1)
- R49 pad 2: Net-(C60-Pad1) -> Net-(Q13-Pad1)
- R5 pad 1: /CoreSheet/STM32F103_SIG_LED_1 -> /PFC_GATE_HIGH_1
- R5 pad 2: Net-(D2-Pad2) -> /PFC_VCC_DUT_1
- R50 pad 1: Net-(C61-Pad1) -> Net-(Q13-Pad3)
- R50 pad 2: Net-(Q11-Pad3) -> Net-(Q13-Pad1)
- R51 pad 2: Net-(R51-Pad2) -> Net-(Q13-Pad3)
- R52 pad 2: Net-(R52-Pad2) -> Net-(Q13-Pad3)
- R53 pad 1: Net-(R51-Pad2) -> /Cell_1_Sheet/CurrentSource_A_Sheet/PFC_CRNT
- R53 pad 2: /VCC5V -> GNDA
- R54 pad 1: Net-(R54-Pad1) -> /Cell_1_Sheet/CurrentSource_B_Sheet/PFC_CRNT
- R54 pad 2: Net-(Q11-Pad1) -> GNDA
- R55 pad 1: Net-(Q11-Pad3) -> /PFC_GATE_HIGH_2
- R55 pad 2: Net-(Q11-Pad1) -> /PFC_VCC_DUT_2
- R56 pad 1: GNDA -> /PFC_GATE_LOW_2
- R56 pad 2: Net-(Q11-Pad3) -> /VDD3.3V
- R57 pad 1: GNDA -> /PFC_GATE_HIGH_3
- R57 pad 2: Net-(Q11-Pad3) -> /PFC_VCC_DUT_3
- R58 pad 1: Net-(C72-Pad1) -> /PFC_GATE_LOW_3
- R58 pad 2: /VCC5V -> /VDD3.3V
- R59 pad 1: Net-(C73-Pad1) -> /PFC_STOP_3
- R59 pad 2: /VCC5V -> Net-(Q16-Pad1)
- R6 pad 1: /CoreSheet/STM32F103_SIG_LED_2 -> /PFC_GATE_LOW_1
- R6 pad 2: Net-(D3-Pad2) -> /VDD3.3V
- R60 pad 1: Net-(C74-Pad2) -> Net-(Q16-Pad1)
- R61 pad 1: Net-(C75-Pad2) -> Net-(C39-Pad1)
- R61 pad 2: GNDA -> /VCC5V
- R62 pad 1: Net-(Q12-Pad1) -> Net-(C40-Pad2)
- R62 pad 2: Net-(C74-Pad1) -> GNDA
- R63 pad 1: Net-(Q13-Pad1) -> Net-(Q17-Pad1)
- R63 pad 2: Net-(C75-Pad1) -> Net-(C40-Pad1)
- R65 pad 1: /U_PFC_VCC_ADJ -> /VCC30V
- R65 pad 2: GNDA -> Net-(Q17-Pad3)
- R66 pad 1: /VCC30V -> Net-(Q18-Pad1)
- R66 pad 2: Net-(Q12-Pad2) -> Net-(C44-Pad1)
- R67 pad 1: /VCC30V -> Net-(Q19-Pad1)
- R67 pad 2: Net-(Q13-Pad2) -> Net-(C45-Pad1)
- R68 pad 1: Net-(Q14-Pad1) -> Net-(C45-Pad2)
- R68 pad 2: Net-(C82-Pad1) -> GNDA
- R69 pad 1: Net-(Q15-Pad1) -> /PFC_VCC_DUT_3
- R69 pad 2: Net-(C84-Pad1) -> Net-(C45-Pad2)
- R7 pad 1: /CoreSheet/STM32F103_SIG_LED_3 -> /PFC_STOP_1
- R7 pad 2: Net-(D4-Pad2) -> Net-(Q3-Pad1)
- R70 pad 1: Net-(Q16-Pad1) -> /VCC30V
- R70 pad 2: Net-(C83-Pad1) -> Net-(C44-Pad2)
- R71 pad 1: Net-(Q17-Pad1) -> Net-(Q20-Pad1)
- R71 pad 2: Net-(C85-Pad1) -> Net-(C46-Pad1)
- R72 pad 1: Net-(C84-Pad2) -> /VCC30V
- R72 pad 2: GNDA -> Net-(Q20-Pad3)
- R73 pad 1: Net-(C85-Pad2) -> Net-(C46-Pad2)
- R74 pad 1: /PFC_VCC_DUT_2 -> Net-(C47-Pad2)
- R74 pad 2: Net-(C84-Pad2) -> Net-(C46-Pad2)
- R75 pad 1: /PFC_VCC_DUT_3 -> Net-(C48-Pad1)
- R75 pad 2: Net-(C85-Pad2) -> Net-(C47-Pad2)
- R76 pad 1: /VCC30V -> /PFC_STOP_2
- R76 pad 2: Net-(C82-Pad2) -> Net-(Q21-Pad1)
- R77 pad 1: /VCC30V -> Net-(Q21-Pad1)
- R77 pad 2: Net-(C83-Pad2) -> GNDA
- R78 pad 1: Net-(Q18-Pad1) -> Net-(C49-Pad1)
- R78 pad 2: Net-(C86-Pad1) -> /VCC5V
- R79 pad 1: Net-(Q19-Pad1) -> Net-(C50-Pad2)
- R79 pad 2: Net-(C87-Pad1) -> GNDA
- R8 pad 1: /CoreSheet/STM32F103_BTN_1 -> Net-(Q3-Pad1)
- R8 pad 2: Net-(R8-Pad2) -> GNDA
- R80 pad 1: /VCC30V -> Net-(Q22-Pad1)
- R80 pad 2: Net-(Q18-Pad2) -> Net-(C50-Pad1)
- R81 pad 1: Net-(C86-Pad2) -> /U_PFC_VCC_ADJ
- R82 pad 2: Net-(Q19-Pad2) -> Net-(Q22-Pad3)
- R83 pad 1: Net-(C87-Pad2) -> Net-(Q23-Pad1)
- R83 pad 2: GNDA -> Net-(C54-Pad1)
- R84 pad 1: Net-(C88-Pad2) -> Net-(Q24-Pad1)
- R84 pad 2: Net-(C86-Pad2) -> Net-(C55-Pad1)
- R85 pad 1: Net-(C89-Pad2) -> Net-(C55-Pad2)
- R85 pad 2: Net-(C87-Pad2) -> GNDA
- R86 pad 1: Net-(C90-Pad1) -> /PFC_VCC_DUT_2
- R86 pad 2: Net-(C88-Pad2) -> Net-(C55-Pad2)
- R87 pad 1: Net-(C91-Pad1) -> /VCC30V
- R87 pad 2: Net-(C89-Pad2) -> Net-(C54-Pad2)
- R88 pad 1: Net-(C88-Pad1) -> Net-(Q25-Pad1)
- R88 pad 2: GNDA -> Net-(C56-Pad1)
- R89 pad 1: Net-(C89-Pad1) -> /VCC30V
- R89 pad 2: GNDA -> Net-(Q25-Pad3)
- R9 pad 1: /CoreSheet/STM32F103_BTN_2 -> Net-(C2-Pad1)
- R9 pad 2: Net-(R9-Pad2) -> /VCC5V
- R90 pad 1: /PFC_GATE_HIGH_2 -> Net-(C56-Pad2)
- R90 pad 2: /PFC_VCC_DUT_2 -> GNDA
- R91 pad 1: /PFC_GATE_LOW_2 -> Net-(C57-Pad2)
- R91 pad 2: /VDD3.3V -> Net-(C56-Pad2)
- R92 pad 1: /PFC_GATE_HIGH_3 -> Net-(C58-Pad1)
- R92 pad 2: /PFC_VCC_DUT_3 -> Net-(C57-Pad2)
- R93 pad 1: /PFC_GATE_LOW_3 -> /U_PFC_FB_OVP_ADJ
- R93 pad 2: /VDD3.3V -> GNDA
- R94 pad 1: /U_PFC_FB_OVP_ADJ -> Net-(Q26-Pad1)
- R94 pad 2: GNDA -> Net-(C60-Pad1)
- R95 pad 1: Net-(Q22-Pad1) -> Net-(C60-Pad2)
- R95 pad 2: Net-(C94-Pad1) -> GNDA
- R96 pad 1: Net-(C94-Pad2) -> /VCC12V
- R96 pad 2: GNDA -> Net-(Q26-Pad2)
- R97 pad 1: /VCC12V -> /PFC_DUT_FB_OVP
- R97 pad 2: Net-(Q22-Pad2) -> Net-(C60-Pad2)
- R98 pad 1: /PFC_DUT_FB_OVP -> /VCC12V
- R98 pad 2: Net-(C94-Pad2) -> Net-(Q26-Pad2)
- R99 pad 2: Net-(Q22-Pad2) -> Net-(Q26-Pad2)
- SW1 pad 1: Net-(R1-Pad2) -> Net-(R109-Pad2)
- SW2 pad 1: Net-(R3-Pad2) -> Net-(R111-Pad2)
- SW3 pad 1: Net-(R8-Pad2) -> Net-(R116-Pad2)
- SW4 pad 1: Net-(R9-Pad2) -> Net-(R117-Pad2)
- U1 pad 1: /VDD3.3V -> /ADS1118_SCK
- U1 pad 10: /CoreSheet/STM32F103_SIG_LED_2 -> /ADS1118_MOSI
- U1 pad 2: /CoreSheet/STM32F103_BTN_0 -> /ADS1118_NCS_0
- U1 pad 3: /CoreSheet/STM32F103_BTN_1 -> GNDA
- U1 pad 4: /CoreSheet/STM32F103_BTN_2 -> /Cell_0_Sheet/CurrentSource_A_Sheet/PFC_CRNT
- U1 pad 5: Net-(C27-Pad1) -> GNDA
- U1 pad 6: Net-(C24-Pad1) -> /Cell_0_Sheet/CurrentSource_B_Sheet/PFC_CRNT
- U1 pad 7: Net-(R1-Pad2) -> GNDA
- U1 pad 8: /CoreSheet/STM32F103_SIG_LED_0 -> Net-(C1-Pad1)
- U1 pad 9: /CoreSheet/STM32F103_SIG_LED_1 -> /ADS1118_MISO
- U10 pad 1: Net-(D7-Pad1) -> /ADS1118_SCK
- U10 pad 2: (no net) -> /ADS1118_NCS_1
- U10 pad 4: Net-(C60-Pad1) -> /Cell_1_Sheet/CurrentSource_A_Sheet/PFC_CRNT
- U10 pad 5: Net-(R51-Pad2) -> GNDA
- U10 pad 6: Net-(C63-Pad1) -> /Cell_1_Sheet/CurrentSource_B_Sheet/PFC_CRNT
- U10 pad 8: /VCC12V -> Net-(C38-Pad1)
- U10 pad 9: GNDA -> /ADS1118_MISO
- U11 pad 1: Net-(C61-Pad1) -> Net-(C40-Pad1)
- U11 pad 2: Net-(C56-Pad1) -> Net-(C40-Pad2)
- U11 pad 3: Net-(R47-Pad1) -> Net-(C39-Pad1)
- U11 pad 4: GNDA -> /VCC30V
- U11 pad 5: GNDA -> /U_PFC_VCC_ADJ
- U11 pad 6: Net-(R54-Pad1) -> Net-(C45-Pad2)
- U11 pad 7: Net-(R52-Pad2) -> Net-(C45-Pad1)
- U11 pad 8: /VCC12V -> Net-(C46-Pad1)
- U12 pad 1: GNDA -> Net-(C44-Pad1)
- U12 pad 2: /VDD3.3V -> GNDA
- U12 pad 3: /VCC5V -> Net-(Q17-Pad3)
- U13 pad 1: GNDA -> Net-(C50-Pad1)
- U13 pad 2: /VDD1.25V -> Net-(C50-Pad2)
- U13 pad 3: /VCC5V -> Net-(C49-Pad1)
- U14 pad 1: Net-(C74-Pad1) -> Net-(C54-Pad1)
- U14 pad 2: Net-(C74-Pad2) -> GNDA
- U14 pad 3: Net-(C72-Pad1) -> Net-(Q22-Pad3)
- U14 pad 4: /VCC30V -> Net-(C54-Pad2)
- U14 pad 5: /U_PFC_VCC_ADJ -> /VCC5V
- U15 pad 1: Net-(C75-Pad1) -> Net-(C60-Pad1)
- U15 pad 2: Net-(C75-Pad2) -> Net-(C60-Pad2)
- U15 pad 3: Net-(C73-Pad1) -> /U_PFC_FB_OVP_ADJ
- U15 pad 4: /VCC30V -> GNDA
- U15 pad 5: /U_PFC_VCC_ADJ -> GNDA
- U15 pad 6: Net-(C85-Pad2) -> GNDA
- U15 pad 7: Net-(C85-Pad1) -> (no net)
- U15 pad 8: Net-(C87-Pad1) -> /VCC12V
- U16 pad 1: Net-(C82-Pad1) -> GNDA
- U16 pad 2: GNDA -> Net-(C63-Pad1)
- U16 pad 3: Net-(Q12-Pad2) -> GNDA
- U16 pad 4: Net-(C82-Pad2) -> Net-(R100-Pad2)
- U16 pad 5: /VCC5V -> (no net)
- U17 pad 1: Net-(C83-Pad1) -> GNDA
- U17 pad 2: GNDA -> Net-(C66-Pad1)
- U17 pad 3: Net-(Q13-Pad2) -> GNDA
- U17 pad 4: Net-(C83-Pad2) -> Net-(R102-Pad2)
- U17 pad 5: /VCC5V -> (no net)
- U18 pad 1: /ADS1118_SCK -> GNDA
- U18 pad 2: /ADS1118_NCS_1 -> Net-(C69-Pad1)
- U18 pad 4: Net-(C88-Pad1) -> Net-(R104-Pad2)
- U18 pad 5: GNDA -> (no net)
- U18 pad 6: Net-(C89-Pad1) -> Net-(R104-Pad2)
- U18 pad 7: GNDA -> /PFC_VCC_DUT_3
- U18 pad 8: Net-(C92-Pad1) -> /PFC_GATE_HIGH_3
- U19 pad 1: Net-(C94-Pad1) -> GNDA
- U19 pad 2: Net-(C94-Pad2) -> Net-(C72-Pad1)
- U19 pad 3: /U_PFC_FB_OVP_ADJ -> GNDA
- U19 pad 4: GNDA -> Net-(R106-Pad2)
- U19 pad 5: GNDA -> (no net)
- U19 pad 6: GNDA -> Net-(R106-Pad2)
- U19 pad 7: (no net) -> /PFC_VCC_DUT_1
- U19 pad 8: /VCC12V -> /PFC_GATE_HIGH_1
- U2 pad 1: /ADS1118_MOSI -> Net-(C3-Pad1)
- U2 pad 10: (no net) -> Net-(C7-Pad2)
- U2 pad 11: (no net) -> GNDA
- U2 pad 12: (no net) -> Net-(C11-Pad1)
- U2 pad 13: GNDA -> /Cell_0_Sheet/CurrentSource_B_Sheet/PFC_CRNT
- U2 pad 14: /CoreSheet/XC6SLX9_CLK -> /Cell_0_Sheet/CurrentSource_B_Sheet/PFC_CRNT
- U2 pad 2: /ADS1118_MISO -> Net-(C3-Pad2)
- U2 pad 3: GNDA -> Net-(C2-Pad1)
- U2 pad 4: /VDD3.3V -> /VCC30V
- U2 pad 5: /ADS1118_SCK -> /U_PFC_VCC_ADJ
- U2 pad 6: /ADS1118_NCS_0 -> Net-(C8-Pad2)
- U2 pad 7: /ADS1118_NCS_1 -> Net-(C8-Pad1)
- U2 pad 8: (no net) -> Net-(C9-Pad1)
- U2 pad 9: (no net) -> Net-(C9-Pad2)
- U20 pad 1: GNDA -> /VDD3.3V
- U20 pad 2: Net-(C97-Pad1) -> /CoreSheet/STM32F103_BTN_0
- U20 pad 3: GNDA -> /CoreSheet/STM32F103_BTN_1
- U20 pad 4: Net-(R101-Pad2) -> /CoreSheet/STM32F103_BTN_2
- U20 pad 5: (no net) -> Net-(C100-Pad1)
- U20 pad 6: Net-(R101-Pad2) -> Net-(C97-Pad1)
- U20 pad 7: /PFC_VCC_DUT_0 -> Net-(R109-Pad2)
- U20 pad 8: /PFC_GATE_HIGH_0 -> /CoreSheet/STM32F103_SIG_LED_0
- U21 pad 1: GNDA -> (no net)
- U21 pad 2: Net-(C100-Pad1) -> (no net)
- U21 pad 4: Net-(R103-Pad2) -> /VDD3.3V
- U21 pad 6: Net-(R103-Pad2) -> /ADS1118_NCS_0
- U21 pad 7: /PFC_VCC_DUT_2 -> /ADS1118_NCS_1
- U21 pad 8: /PFC_GATE_HIGH_2 -> (no net)
- U22 pad 1: GNDA -> /CoreSheet/W25Q32_NCS
- U22 pad 2: Net-(C103-Pad1) -> /CoreSheet/XC6SLX9_W25Q32_MISO
- U22 pad 3: GNDA -> /CoreSheet/W25Q32_NWP
- U22 pad 4: Net-(R105-Pad2) -> GNDA
- U22 pad 5: (no net) -> /CoreSheet/XC6SLX9_W25Q32_MOSI
- U22 pad 6: Net-(R105-Pad2) -> /CoreSheet/XC6SLX9_W25Q32_SCK
- U22 pad 7: /PFC_VCC_DUT_3 -> /CoreSheet/W25Q32_HOLD
- U22 pad 8: /PFC_GATE_HIGH_3 -> /VDD3.3V
- U23 pad 1: GNDA -> /U_PFC_FB_OVP_ADJ
- U23 pad 2: Net-(C106-Pad1) -> /U_PFC_FB_OVP_ADJ
- U23 pad 3: GNDA -> /CoreSheet/U_PFC_FB_OVP_ADJ_DAC
- U23 pad 4: Net-(R107-Pad2) -> GNDA
- U23 pad 5: (no net) -> /CoreSheet/U_PFC_VCC_ADJ_DAC
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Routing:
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- added copper zone on In1.Cu, net GNDA
- added copper zone on In2.Cu, net GNDA
- removed copper zone on B.Cu, net /VCC12V
- removed copper zone on F.Cu, net /VCC5V
- removed copper zone on B.Cu, net /VDD1.25V
- removed copper zone on F.Cu, net Net-(D8-Pad2)
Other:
- board size 85 x 115 mm -> 78 x 109 mm
- copper layers 2 -> 4
